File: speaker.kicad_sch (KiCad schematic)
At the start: 18 parts, among them SW1 SW_DIP_x08

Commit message: Upgrade to KiCAD 9.0
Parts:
- SP-Plug: value (none) -> (none)

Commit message: drc: updated symbols
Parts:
- SP-Plug: value (none) -> ~
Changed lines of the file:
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@@
 		(dnp no)
 		(fields_autoplaced yes)
-		(property "Reference" "#PWR?"
+		(property "Reference" "#PWR0162"
 			(at 203.2 44.45 0)
 			(effects
@@
 			(project "ceda"
 				(path "/12a6dbe3-008d-4c5b-88f6-9f1c816060be/ef850a34-fb31-4ec2-8b90-4e6ea535ae17"
-					(reference "#PWR?")
+					(reference "#PWR0162")
 					(unit 1)
 				)
@@
 		(dnp no)
 		(fields_autoplaced yes)
-		(property "Reference" "#PWR?"
+		(property "Reference" "#PWR0175"
 			(at 77.47 77.47 0)
 			(effects
@@
 			(project "ceda"
 				(path "/12a6dbe3-008d-4c5b-88f6-9f1c816060be/ef850a34-fb31-4ec2-8b90-4e6ea535ae17"
-					(reference "#PWR?")
+					(reference "#PWR0175")
 					(unit 1)
 				)
@@
 	)
 	(symbol
-		(lib_name "GND_1")
 		(lib_id "power:GND")
 		(at 31.75 191.77 0)
@@
 		(dnp no)
 		(fields_autoplaced yes)
-		(property "Reference" "#PWR?"
+		(property "Reference" "#PWR0173"
 			(at 77.47 29.21 0)
 			(effects
@@
 			(project "ceda"
 				(path "/12a6dbe3-008d-4c5b-88f6-9f1c816060be/ef850a34-fb31-4ec2-8b90-4e6ea535ae17"
-					(reference "#PWR?")
+					(reference "#PWR0173")
 					(unit 1)
 				)
@@
 			)
 		)
-		(property "Value" ""
+		(property "Value" "~"
 			(at 250.9012 81.7122 0)
 			(effects
@@
 		(dnp no)
 		(fields_autoplaced yes)
-		(property "Reference" "#PWR?"
+		(property "Reference" "#PWR0167"
 			(at 90.17 144.78 0)
 			(effects
@@
 			(project "ceda"
 				(path "/12a6dbe3-008d-4c5b-88f6-9f1c816060be/ef850a34-fb31-4ec2-8b90-4e6ea535ae17"
-					(reference "#PWR?")
+					(reference "#PWR0167")
 					(unit 1)
 				)
@@
 		(dnp no)
 		(fields_autoplaced yes)
-		(property "Reference" "#PWR?"
+		(property "Reference" "#PWR0163"
 			(at 203.2 102.87 0)
 			(effects
@@
 			(project "ceda"
 				(path "/12a6dbe3-008d-4c5b-88f6-9f1c816060be/ef850a34-fb31-4ec2-8b90-4e6ea535ae17"
-					(reference "#PWR?")
+					(reference "#PWR0163")
 					(unit 1)
 				)
@@
 		(dnp no)
 		(fields_autoplaced yes)
-		(property "Reference" "#PWR?"
+		(property "Reference" "#PWR0165"
 			(at 180.34 55.88 0)
 			(effects
@@
 			(project "ceda"
 				(path "/12a6dbe3-008d-4c5b-88f6-9f1c816060be/ef850a34-fb31-4ec2-8b90-4e6ea535ae17"
-					(reference "#PWR?")
+					(reference "#PWR0165")
 					(unit 1)
 				)
@@
 		(dnp no)
 		(fields_autoplaced yes)
-		(property "Reference" "#PWR?"
+		(property "Reference" "#PWR0179"
 			(at 222.25 43.18 0)
 			(effects
@@
 			(project "ceda"
 				(path "/12a6dbe3-008d-4c5b-88f6-9f1c816060be/ef850a34-fb31-4ec2-8b90-4e6ea535ae17"
-					(reference "#PWR?")
+					(reference "#PWR0179")
 					(unit 1)
 				)
@@
 		(dnp no)
 		(fields_autoplaced yes)
-		(property "Reference" "#PWR?"
+		(property "Reference" "#PWR0177"
 			(at 232.41 97.79 0)
 			(effects
@@
 			(project "ceda"
 				(path "/12a6dbe3-008d-4c5b-88f6-9f1c816060be/ef850a34-fb31-4ec2-8b90-4e6ea535ae17"
-					(reference "#PWR?")
+					(reference "#PWR0177")
 					(unit 1)
 				)
@@
 		(dnp no)
 		(fields_autoplaced yes)
-		(property "Reference" "#PWR?"
+		(property "Reference" "#PWR0178"
 			(at 245.11 74.93 0)
 			(effects
@@
 			(project "ceda"
 				(path "/12a6dbe3-008d-4c5b-88f6-9f1c816060be/ef850a34-fb31-4ec2-8b90-4e6ea535ae17"
-					(reference "#PWR?")
-					(unit 1)
-				)
+					(reference "#PWR0178")
+					(unit 1)
+				)

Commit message: drc: fixed labels
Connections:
- net D7: now reaches UA11.11 (Y7)
- net D6: now reaches UA11.12 (Y6)
- net D5: now reaches UA11.13 (Y5)
- net D4: now reaches UA11.14 (Y4)
- net D3: now reaches UA11.15 (Y3)
- net D2: now reaches UA11.16 (Y2)
- net D1: now reaches UA11.17 (Y1)
- net D0: now reaches UA11.18 (Y0)
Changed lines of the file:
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@@
 	(wire
 		(pts
-			(xy 20.32 99.06) (xy 64.77 99.06)
+			(xy 26.67 99.06) (xy 64.77 99.06)
 		)
 		(stroke
@@
 		)
 	)
+	(label "D0"
+		(at 104.14 148.59 0)
+		(effects
+			(font
+				(size 1.27 1.27)
+			)
+			(justify left bottom)
+		)
+	)
 	(label "~{SPEAKER_CS}"
 		(at 175.26 45.72 0)
@@
 		)
 	)
-	(label "~{RD|WR}"
-		(at 20.32 99.06 0)
-		(effects
-			(font
-				(size 1.27 1.27)
-			)
-			(justify left bottom)
-		)
-	)
 	(label "A3"
 		(at 59.69 86.36 0)
+		(effects
+			(font
+				(size 1.27 1.27)
+			)
+			(justify left bottom)
+		)
+	)
+	(label "D5"
+		(at 104.14 161.29 0)
+		(effects
+			(font
+				(size 1.27 1.27)
+			)
+			(justify left bottom)
+		)
+	)
+	(label "D4"
+		(at 104.14 158.75 0)
+		(effects
+			(font
+				(size 1.27 1.27)
+			)
+			(justify left bottom)
+		)
+	)
+	(label "D6"
+		(at 104.14 163.83 0)
+		(effects
+			(font
+				(size 1.27 1.27)
+			)
+			(justify left bottom)
+		)
+	)
+	(label "D3"
+		(at 104.14 156.21 0)
+		(effects
+			(font
+				(size 1.27 1.27)
+			)
+			(justify left bottom)
+		)
+	)
+	(label "D7"
+		(at 104.14 166.37 0)
+		(effects
+			(font
+				(size 1.27 1.27)
+			)
+			(justify left bottom)
+		)
+	)
+	(label "D1"
+		(at 104.14 151.13 0)
+		(effects
+			(font
+				(size 1.27 1.27)
+			)
+			(justify left bottom)
+		)
+	)
+	(label "D2"
+		(at 104.14 153.67 0)
 		(effects
 			(font
@@
 		)
 	)
+	(global_label "~{RD|WR}"
+		(shape input)
+		(at 26.67 99.06 180)
+		(fields_autoplaced yes)
+		(effects
+			(font
+				(size 1.27 1.27)
+			)
+			(justify right)
+		)
+		(property "Intersheetrefs" "${INTERSHEET_REFS}"
+			(at 17.2139 99.06 0)
+			(effects
+				(font
+					(size 1.27 1.27)
+				)
+				(justify right)
+				(hide yes)
+			)
+		)
+	)
 	(global_label "~{GPIO_CS}"
 		(shape output)
@@
 		)
 	)
-	(hierarchical_label "DATA"
+	(hierarchical_label "D[7..0]"
 		(shape bidirectional)
 		(at 113.03 171.45 0)

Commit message: Annotated all components
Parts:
- renumbered SP-Plug to SP-Plug1, SP-Socket to SP-Socket1
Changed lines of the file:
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@@
+		)
+	)
+	(label "D5"
+		(at 104.14 161.29 0)
+		(effects
+			(font
+				(size 1.27 1.27)
+			)
+			(justify left bottom)
 		)
 	)
@@
 		)
 	)
+	(label "D2"
+		(at 104.14 153.67 0)
+		(effects
+			(font
+				(size 1.27 1.27)
+			)
+			(justify left bottom)
+		)
+	)
 	(label "~{SPEAKER_CS}"
 		(at 175.26 45.72 0)
@@
 		)
 	)
+	(label "D7"
+		(at 104.14 166.37 0)
+		(effects
+			(font
+				(size 1.27 1.27)
+			)
+			(justify left bottom)
+		)
+	)
 	(label "A7"
 		(at 59.69 45.72 0)
@@
 		)
 	)
+	(label "D4"
+		(at 104.14 158.75 0)
+		(effects
+			(font
+				(size 1.27 1.27)
+			)
+			(justify left bottom)
+		)
+	)
 	(label "~{DIPSW_CS}"
 		(at 67.31 171.45 0)
@@
 		)
 	)
+	(label "D3"
+		(at 104.14 156.21 0)
+		(effects
+			(font
+				(size 1.27 1.27)
+			)
+			(justify left bottom)
+		)
+	)
+	(label "D1"
+		(at 104.14 151.13 0)
+		(effects
+			(font
+				(size 1.27 1.27)
+			)
+			(justify left bottom)
+		)
+	)
 	(label "A1"
 		(at 59.69 81.28 0)
@@
 		)
 	)
-	(label "D5"
-		(at 104.14 161.29 0)
-		(effects
-			(font
-				(size 1.27 1.27)
-			)
-			(justify left bottom)
-		)
-	)
-	(label "D4"
-		(at 104.14 158.75 0)
-		(effects
-			(font
-				(size 1.27 1.27)
-			)
-			(justify left bottom)
-		)
-	)
 	(label "D6"
 		(at 104.14 163.83 0)
-		(effects
-			(font
-				(size 1.27 1.27)
-			)
-			(justify left bottom)
-		)
-	)
-	(label "D3"
-		(at 104.14 156.21 0)
-		(effects
-			(font
-				(size 1.27 1.27)
-			)
-			(justify left bottom)
-		)
-	)
-	(label "D7"
-		(at 104.14 166.37 0)
-		(effects
-			(font
-				(size 1.27 1.27)
-			)
-			(justify left bottom)
-		)
-	)
-	(label "D1"
-		(at 104.14 151.13 0)
-		(effects
-			(font
-				(size 1.27 1.27)
-			)
-			(justify left bottom)
-		)
-	)
-	(label "D2"
-		(at 104.14 153.67 0)
 		(effects
 			(font
@@
 		(dnp no)
 		(fields_autoplaced yes)
-		(property "Reference" "SP-Plug"
+		(property "Reference" "SP-Plug1"
 			(at 250.9012 79.1753 0)
 			(effects
@@
 			(project "ceda"
 				(path "/12a6dbe3-008d-4c5b-88f6-9f1c816060be/ef850a34-fb31-4ec2-8b90-4e6ea535ae17"
-					(reference "SP-Plug")
+					(reference "SP-Plug1")
 					(unit 1)
 				)
@@
 		(dnp no)
 		(fields_autoplaced yes)
-		(property "Reference" "SP-Socket"
+		(property "Reference" "SP-Socket1"
 			(at 262.255 77.12 0)
 			(effects
@@
 			(project "ceda"
 				(path "/12a6dbe3-008d-4c5b-88f6-9f1c816060be/ef850a34-fb31-4ec2-8b90-4e6ea535ae17"
-					(reference "SP-Socket")
-					(unit 1)
-				)
+					(reference "SP-Socket1")
+					(unit 1)
+				)

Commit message: Assigned default footprints to ICs
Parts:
- UA11: footprint (none) -> Package_DIP:DIP-20_W7.62mm
- UC7, UF16: footprint (none) -> Package_DIP:DIP-14_W7.62mm
- UD8, UD9: footprint (none) -> Package_DIP:DIP-16_W7.62mm
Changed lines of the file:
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@@
 			)
 		)
-		(property "Footprint" ""
+		(property "Footprint" "Package_DIP:DIP-16_W7.62mm"
 			(at 77.47 88.9 0)
 			(effects
@@
 			)
 		)
-		(property "Footprint" ""
+		(property "Footprint" "Package_DIP:DIP-16_W7.62mm"
 			(at 77.47 40.64 0)
 			(effects
@@
 			)
 		)
-		(property "Footprint" ""
+		(property "Footprint" "Package_DIP:DIP-20_W7.62mm"
 			(at 90.17 161.29 0)
 			(effects
@@
 			)
 		)
-		(property "Footprint" ""
+		(property "Footprint" "Package_DIP:DIP-14_W7.62mm"
 			(at 38.1 93.98 0)
 			(effects
@@
 			)
 		)
-		(property "Footprint" ""
+		(property "Footprint" "Package_DIP:DIP-14_W7.62mm"
 			(at 203.2 50.8 0)
 			(effects
@@
 			)
 		)
-		(property "Footprint" ""
+		(property "Footprint" "Package_DIP:DIP-14_W7.62mm"
 			(at 203.2 109.22 0)
 			(effects

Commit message: Fixed some wrong labels
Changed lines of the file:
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@@
+		)
+	)
+	(global_label "D[7..0]"
+		(shape bidirectional)
+		(at 113.03 171.45 0)
+		(fields_autoplaced yes)
+		(effects
+			(font
+				(size 1.27 1.27)
+			)
+			(justify left)
+		)
+		(property "Intersheetrefs" "${INTERSHEET_REFS}"
+			(at 123.7185 171.45 0)
+			(effects
+				(font
+					(size 1.27 1.27)
+				)
+				(justify left)
+				(hide yes)
+			)
 		)
 	)
@@
 		)
 	)
-	(hierarchical_label "D[7..0]"
-		(shape bidirectional)
-		(at 113.03 171.45 0)
-		(effects
-			(font
-				(size 1.27 1.27)
-			)
-			(justify left)
-		)
-	)

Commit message: Fixed wrong labels and connections, added footprint for dip switch
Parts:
- SW1: footprint (none) -> Button_Switch_THT:SW_DIP_SPSTx08_Slide_9.78x22.5mm_W7.62mm_P2.54mm
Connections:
- net at RM2.2 (R1), UA11.2 (A0): now also SW1.9; no longer SW1.16
- net at RM2.3 (R2), UA11.3 (A1): now also SW1.10; no longer SW1.15
- net at RM2.4 (R3), UA11.4 (A2): now also SW1.11; no longer SW1.14
- net at RM2.5 (R4), UA11.5 (A3): now also SW1.12; no longer SW1.13
- net at RM2.6 (R5), UA11.6 (A4): now also SW1.13; no longer SW1.12
- net at RM2.7 (R6), UA11.7 (A5): now also SW1.14; no longer SW1.11
- net at RM2.8 (R7), UA11.8 (A6): now also SW1.15; no longer SW1.10
- net at RM2.9 (R8): no longer SW1.9
- no-connect marks 3 -> 5
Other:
- moved on the sheet: SW1
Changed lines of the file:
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@@
 		(at 90.17 86.36)
 	)
+	(no_connect
+		(at 49.53 168.91)
+	)
+	(no_connect
+		(at 49.53 144.78)
+	)
 	(bus_entry
 		(at 106.68 151.13)
@@
 	(wire
 		(pts
-			(xy 64.77 166.37) (xy 77.47 166.37)
+			(xy 72.39 166.37) (xy 77.47 166.37)
 		)
 		(stroke
@@
 	(wire
 		(pts
-			(xy 49.53 144.78) (xy 49.53 168.91)
-		)
-		(stroke
-			(width 0)
-			(type default)
-		)
-	)
-	(wire
-		(pts
 			(xy 41.91 144.78) (xy 41.91 158.75)
 		)
@@
 		)
 	)
-	(label "disptmg_reg"
-		(at 64.77 166.37 0)
-		(effects
-			(font
-				(size 1.27 1.27)
-			)
-			(justify left bottom)
-		)
-	)
 	(label "~{DIPSW_CS}"
 		(at 102.87 88.9 180)
@@
 		)
 	)
+	(global_label "disptmg_reg"
+		(shape input)
+		(at 72.39 166.37 180)
+		(fields_autoplaced yes)
+		(effects
+			(font
+				(size 1.27 1.27)
+			)
+			(justify right)
+		)
+		(property "Intersheetrefs" "${INTERSHEET_REFS}"
+			(at 57.9145 166.37 0)
+			(effects
+				(font
+					(size 1.27 1.27)
+				)
+				(justify right)
+				(hide yes)
+			)
+		)
+	)
 	(global_label "~{GPIO_CS}"
 		(shape output)
@@
 	(symbol
 		(lib_id "Switch:SW_DIP_x08")
-		(at 41.91 176.53 90)
+		(at 39.37 176.53 270)
+		(mirror x)
 		(unit 1)
 		(exclude_from_sim no)
@@
 		(on_board yes)
 		(dnp no)
-		(fields_autoplaced yes)
 		(property "Reference" "SW1"
-			(at 53.34 175.26 90)
+			(at 27.94 175.26 90)
 			(effects
 				(font
@@
 		)
 		(property "Value" "SW_DIP_x08"
-			(at 53.34 177.8 90)
+			(at 27.94 177.8 90)
 			(effects
 				(font
@@
 			)
 		)
-		(property "Footprint" ""
-			(at 41.91 176.53 0)
+		(property "Footprint" "Button_Switch_THT:SW_DIP_SPSTx08_Slide_9.78x22.5mm_W7.62mm_P2.54mm"
+			(at 39.37 176.53 0)
 			(effects
 				(font
@@
 		)
 		(property "Datasheet" "~"
-			(at 41.91 176.53 0)
+			(at 39.37 176.53 0)
 			(effects
 				(font
@@
 		)
 		(property "Description" ""
-			(at 41.91 176.53 0)
+			(at 39.37 176.53 0)
 			(effects
 				(font

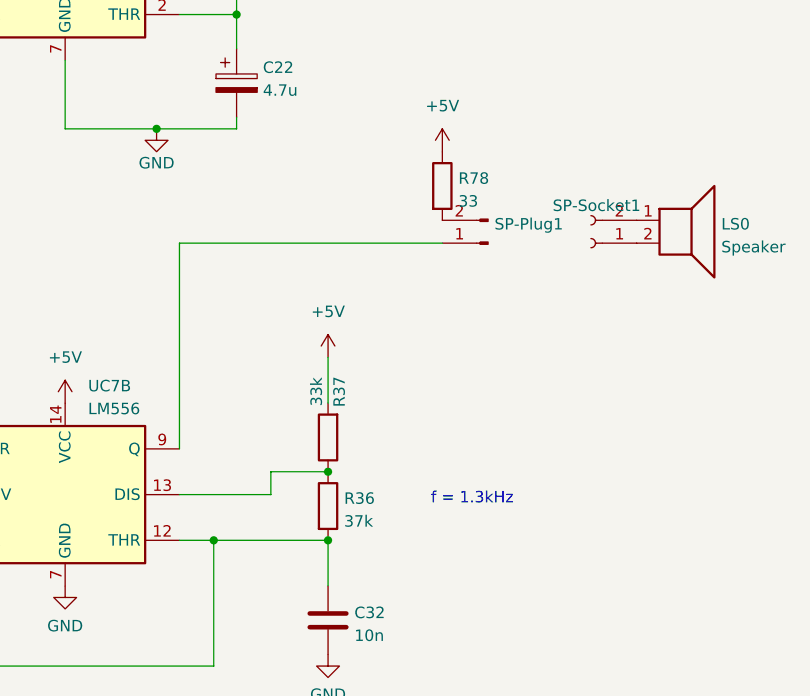
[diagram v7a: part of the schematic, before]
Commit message: pcb: added and placed almost all components
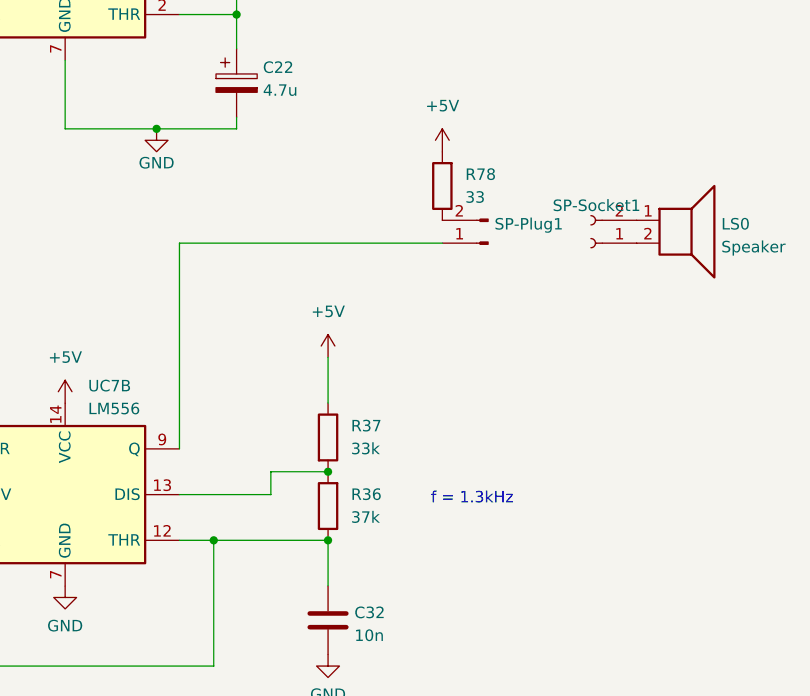
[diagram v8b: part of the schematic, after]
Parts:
- C22: footprint (none) -> Capacitor_THT:CP_Radial_D5.0mm_P2.50mm
- C23, C25, C32: footprint (none) -> Capacitor_THT:C_Disc_D4.3mm_W1.9mm_P5.00mm
- R36, R37, R38: footprint (none) -> Resistor_THT:R_Axial_DIN0204_L3.6mm_D1.6mm_P5.08mm_Vertical
- R78: footprint (none) -> Resistor_THT:R_Axial_DIN0309_L9.0mm_D3.2mm_P12.70mm_Horizontal
- SP-Plug1: footprint (none) -> Connector_Molex:Molex_KK-254_AE-6410-02A_1x02_P2.54mm_Vertical
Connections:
- net +5V: now also R37.1, R78.2; no longer R37.2, R78.1
- net at C32.1, UC7.12 (THR), UC7.8 (TR): now also R36.1; no longer R36.2
- net at SP-Plug1.2 (Pin_2): now also R78.1; no longer R78.2
- new net: R36.2, R37.2, UC7.13 (DIS)
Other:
- moved on the sheet: R36, R37, R78
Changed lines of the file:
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@@
 	(symbol
 		(lib_id "Device:R")
-		(at 232.41 110.49 0)
+		(at 232.41 110.49 180)
 		(unit 1)
 		(exclude_from_sim no)
@@
 		(fields_autoplaced yes)
 		(property "Reference" "R36"
-			(at 234.188 109.6553 0)
-			(effects
-				(font
-					(size 1.27 1.27)
-				)
-				(justify left)
+			(at 234.95 109.2199 0)
+			(effects
+				(font
+					(size 1.27 1.27)
+				)
+				(justify right)
 			)
 		)
 		(property "Value" "37k"
-			(at 234.188 112.1922 0)
-			(effects
-				(font
-					(size 1.27 1.27)
-				)
-				(justify left)
-			)
-		)
-		(property "Footprint" ""
-			(at 230.632 110.49 90)
+			(at 234.95 111.7599 0)
+			(effects
+				(font
+					(size 1.27 1.27)
+				)
+				(justify right)
+			)
+		)
+		(property "Footprint" "Resistor_THT:R_Axial_DIN0204_L3.6mm_D1.6mm_P5.08mm_Vertical"
+			(at 234.188 110.49 90)
 			(effects
 				(font
@@
 	(symbol
 		(lib_id "Device:R")
-		(at 232.41 102.87 180)
-		(unit 1)
-		(exclude_from_sim no)
-		(in_bom yes)
-		(on_board yes)
-		(dnp no)
+		(at 232.41 102.87 0)
+		(unit 1)
+		(exclude_from_sim no)
+		(in_bom yes)
+		(on_board yes)
+		(dnp no)
+		(fields_autoplaced yes)
 		(property "Reference" "R37"
-			(at 233.68 97.79 90)
-			(effects
-				(font
-					(size 1.27 1.27)
-				)
+			(at 234.95 101.5999 0)
+			(effects
+				(font
+					(size 1.27 1.27)
+				)
+				(justify left)
 			)
 		)
 		(property "Value" "33k"
-			(at 231.14 97.79 90)
-			(effects
-				(font
-					(size 1.27 1.27)
-				)
-			)
-		)
-		(property "Footprint" ""
-			(at 234.188 102.87 90)
+			(at 234.95 104.1399 0)
+			(effects
+				(font
+					(size 1.27 1.27)
+				)
+				(justify left)
+			)
+		)
+		(property "Footprint" "Resistor_THT:R_Axial_DIN0204_L3.6mm_D1.6mm_P5.08mm_Vertical"
+			(at 230.632 102.87 90)
 			(effects
 				(font
@@
 	(symbol
 		(lib_id "Device:R")
-		(at 245.11 74.93 0)
+		(at 245.11 74.93 180)
 		(unit 1)
 		(exclude_from_sim no)
@@
 		(fields_autoplaced yes)
 		(property "Reference" "R78"
-			(at 246.888 74.0953 0)
-			(effects
-				(font
-					(size 1.27 1.27)
-				)
-				(justify left)
+			(at 247.65 73.6599 0)
+			(effects
+				(font
+					(size 1.27 1.27)
+				)
+				(justify right)
 			)
 		)
 		(property "Value" "33"
-			(at 246.888 76.6322 0)
-			(effects
-				(font
-					(size 1.27 1.27)
-				)
-				(justify left)
-			)
-		)
-		(property "Footprint" ""
-			(at 243.332 74.93 90)
+			(at 247.65 76.1999 0)
+			(effects
+				(font
+					(size 1.27 1.27)
+				)
+				(justify right)
+			)
+		)
+		(property "Footprint" "Resistor_THT:R_Axial_DIN0309_L9.0mm_D3.2mm_P12.70mm_Horizontal"
+			(at 246.888 74.93 90)
 			(effects
 				(font
@@
 			)
 		)
-		(property "Footprint" ""
+		(property "Footprint" "Resistor_THT:R_Axial_DIN0204_L3.6mm_D1.6mm_P5.08mm_Vertical"
 			(at 220.472 43.18 90)
 			(effects
@@
 			)
 		)
-		(property "Footprint" ""
+		(property "Footprint" "Capacitor_THT:C_Disc_D4.3mm_W1.9mm_P5.00mm"
 			(at 233.3752 127 0)
 			(effects
@@
 			)
 		)
-		(property "Footprint" ""
+		(property "Footprint" "Connector_Molex:Molex_KK-254_AE-6410-02A_1x02_P2.54mm_Vertical"
 			(at 250.19 81.28 0)
 			(effects
@@
 			)
 		)
-		(property "Footprint" ""
+		(property "Footprint" "Capacitor_THT:CP_Radial_D5.0mm_P2.50mm"
 			(at 223.2152 67.31 0)
 			(effects
@@
 			)
 		)
-		(property "Footprint" ""
+		(property "Footprint" "Capacitor_THT:C_Disc_D4.3mm_W1.9mm_P5.00mm"
 			(at 190.5 108.2548 0)
 			(effects
@@
 			)
 		)
-		(property "Footprint" ""
+		(property "Footprint" "Capacitor_THT:C_Disc_D4.3mm_W1.9mm_P5.00mm"
 			(at 190.5 49.8348 0)
 			(effects
